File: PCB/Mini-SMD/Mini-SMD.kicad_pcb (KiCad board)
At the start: 2 copper layers, 65.1 x 96.9 mm, 31 parts, among them J1 Daisy port out, J2 2-pin header, J3 ICSP_ISP6, J4 Daisy port in, K1 HYC77-TF09-200, U1 PC817C-S, U2 ATmega328P-AU, U3 SE5218, U4 TXB0104PWR, Y1 Resonator_GND2

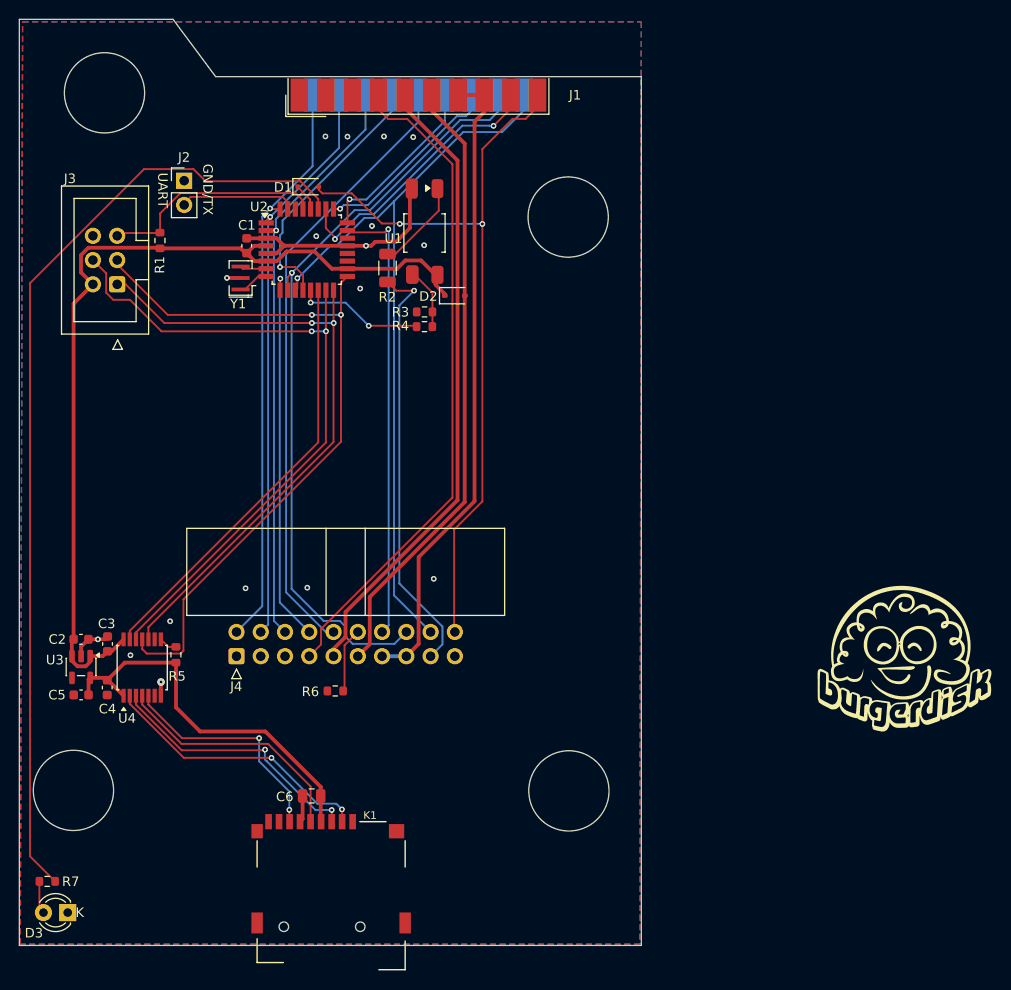
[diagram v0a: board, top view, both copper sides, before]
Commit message: Make PCBs closer to one another
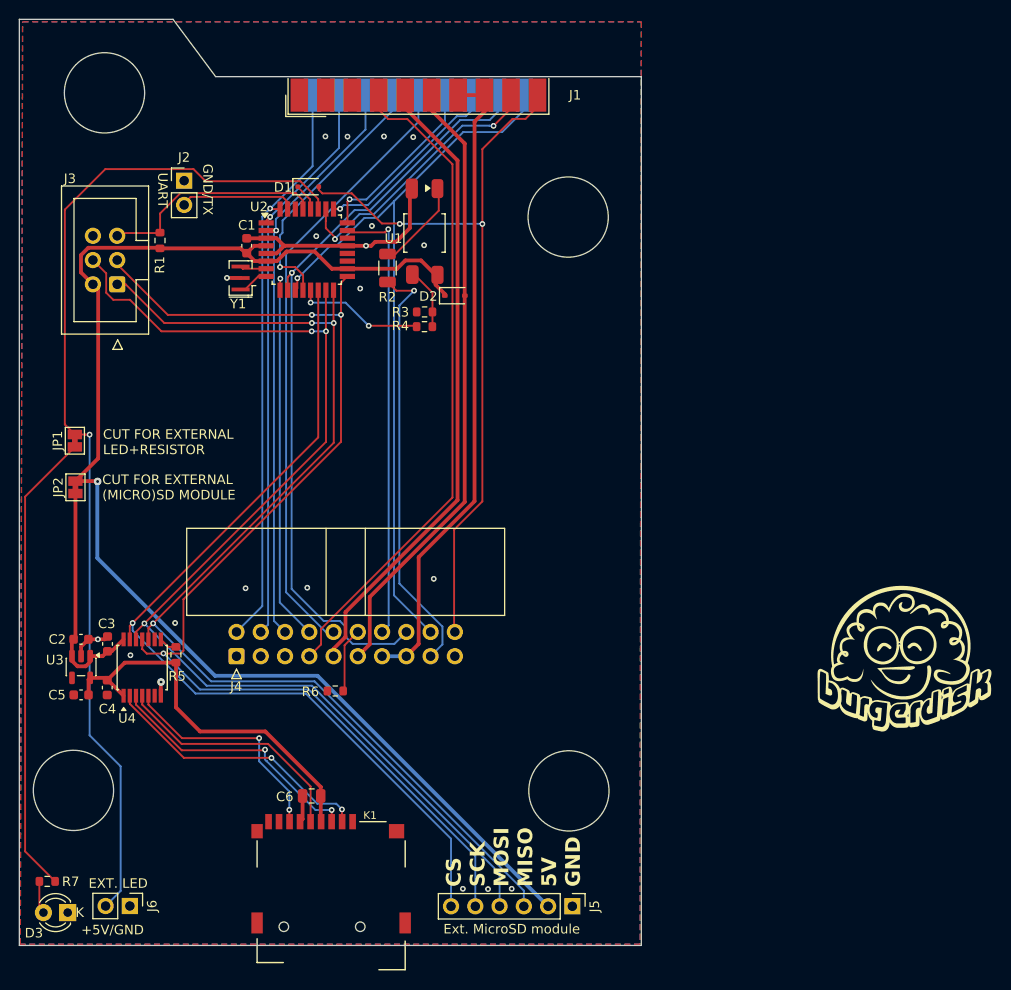
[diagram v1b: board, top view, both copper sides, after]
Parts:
- added J5: Ext. MicroSD module, Connector_PinHeader_2.54mm:PinHeader_1x06_P2.54mm_Vertical, F.Cu at (157.4, 136.2)
- added J6: 2-pin header, Connector_PinHeader_2.54mm:PinHeader_1x02_P2.54mm_Vertical, F.Cu at (111.1, 136.1)
- added JP1: INT/EXT LED JUMPER, Jumper:SolderJumper-2_P1.3mm_Bridged_Pad1.0x1.5mm, F.Cu at (105.3, 87.4)
- added JP2: INT MICROSD JUMPER, Jumper:SolderJumper-2_P1.3mm_Bridged_Pad1.0x1.5mm, F.Cu at (105.4, 92.3)
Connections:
- C2 pad 2: 5V_burgerDisk -> 5V_intMicroSD
- C3 pad 2: 5V_burgerDisk -> 5V_intMicroSD
- R7 pad 2: LED -> Net-(JP1-A)
- U3 pad 1: 5V_burgerDisk -> 5V_intMicroSD
- U3 pad 3: 5V_burgerDisk -> 5V_intMicroSD
- U4 pad 14: 5V_burgerDisk -> 5V_intMicroSD
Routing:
- net MISO: track 68.9 -> 121.0 mm, vias 2 -> 3
- net MOSI: track 73.5 -> 125.0 mm, vias 2 -> 3
- net CS: track 44.7 -> 95.0 mm, vias 0 -> 1
- net Net-(JP1-A): track 0.00 -> 49.5 mm
- net 5V_burgerDisk: track 95.9 -> 143.4 mm, vias 0 -> 1
- net SCK: track 78.0 -> 124.7 mm, vias 2 -> 3
- net 5V_intMicroSD: track 0.00 -> 24.2 mm
- net LED: track 101.2 -> 107.5 mm, vias 0 -> 1
- net GND: vias 17 -> 20
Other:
- board text added: "+5V/GND"
- board text added: "CS SCK MOSI MISO 5V GND"
- board text added: "CUT FOR EXTERNAL (MICRO)SD MODULE"
- board text added: "CUT FOR EXTERNAL LED+RESISTOR"
- board text added: "EXT. LED"
- board text added: "If using an external SD or MicroSD module, cut power to the internal one by cutting the trace in the JP2 jumper. If using an external LED (with external resistor), cut power to the internal one by cutting the trace in the JP1 jumper."

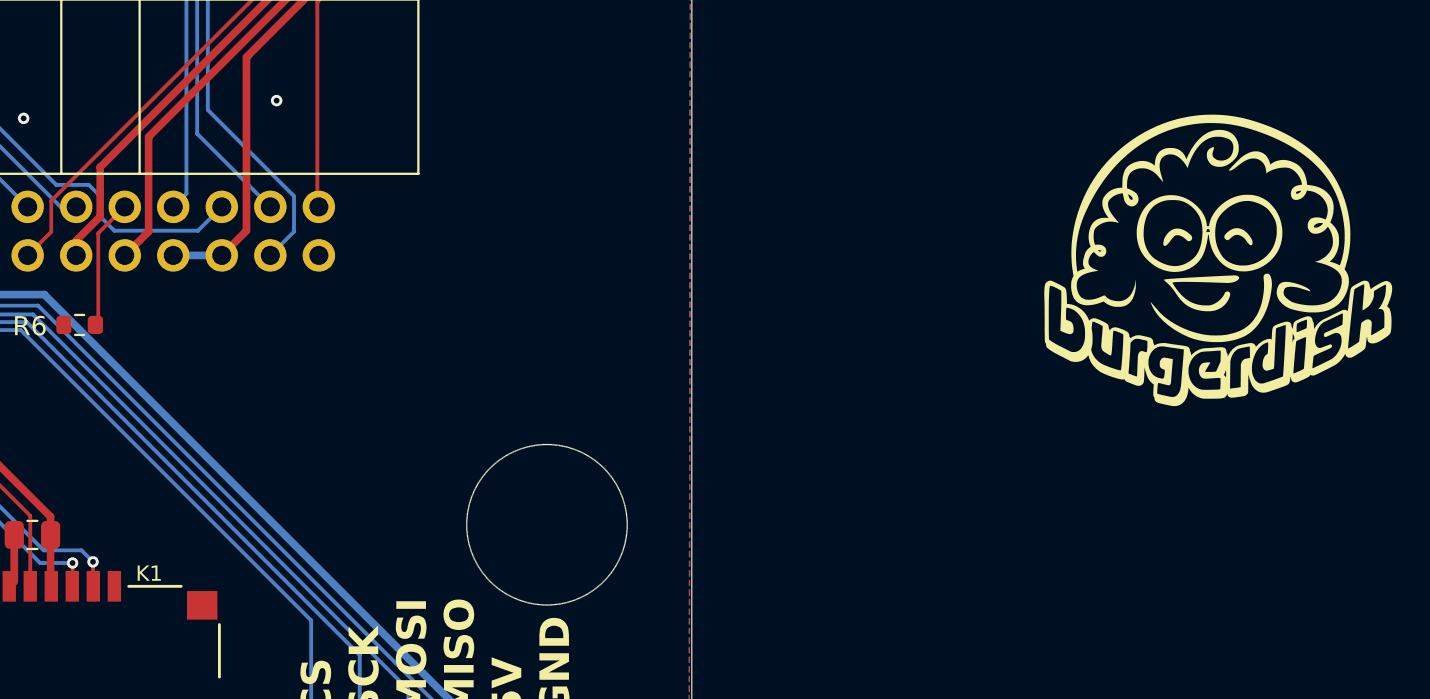
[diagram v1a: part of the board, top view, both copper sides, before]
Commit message: Put the logo back on the PCB
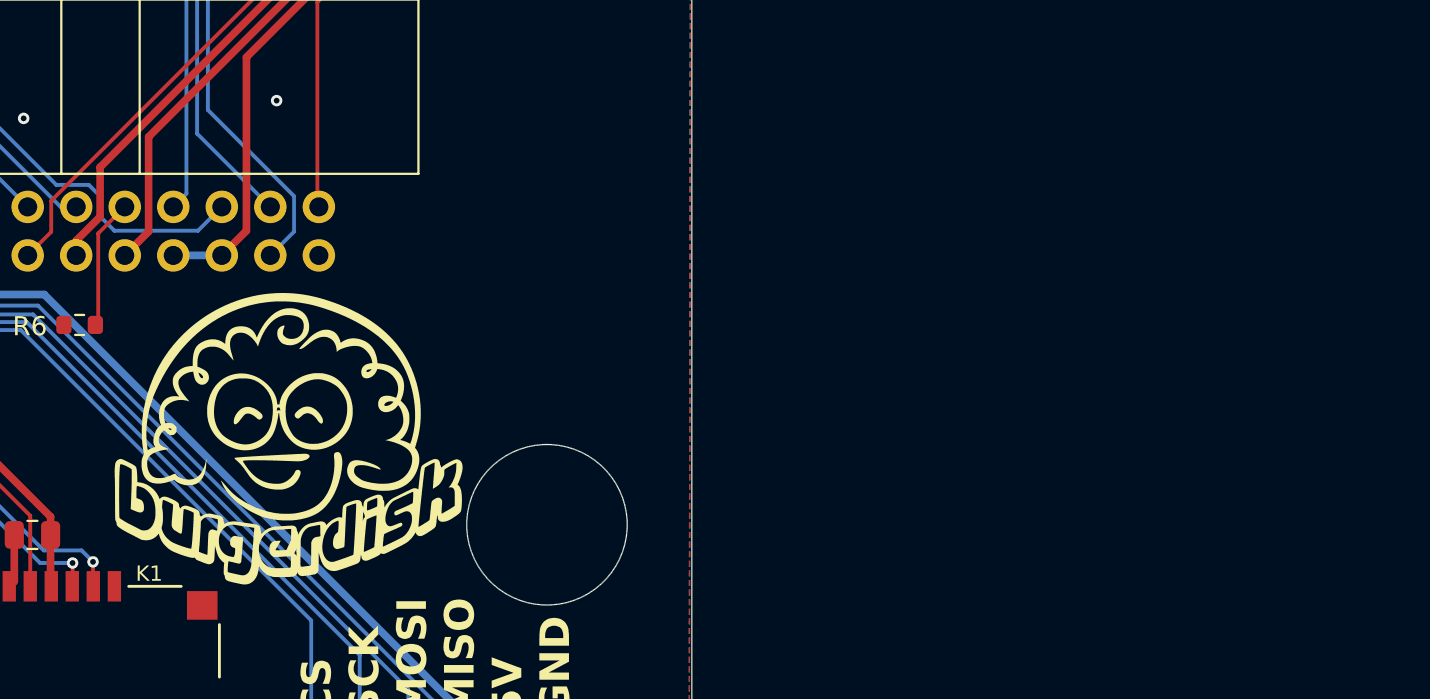
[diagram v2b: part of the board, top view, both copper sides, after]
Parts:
- moved G*** 49.5 mm to (143.5, 119.6)
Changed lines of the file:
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@@
 	(footprint "LOGO"
 		(layer "F.Cu")
-		(at 192.162905 110.299597)
+		(at 143.51 119.634)
 		(property "Reference" "G***"
 			(at 0 0 0)

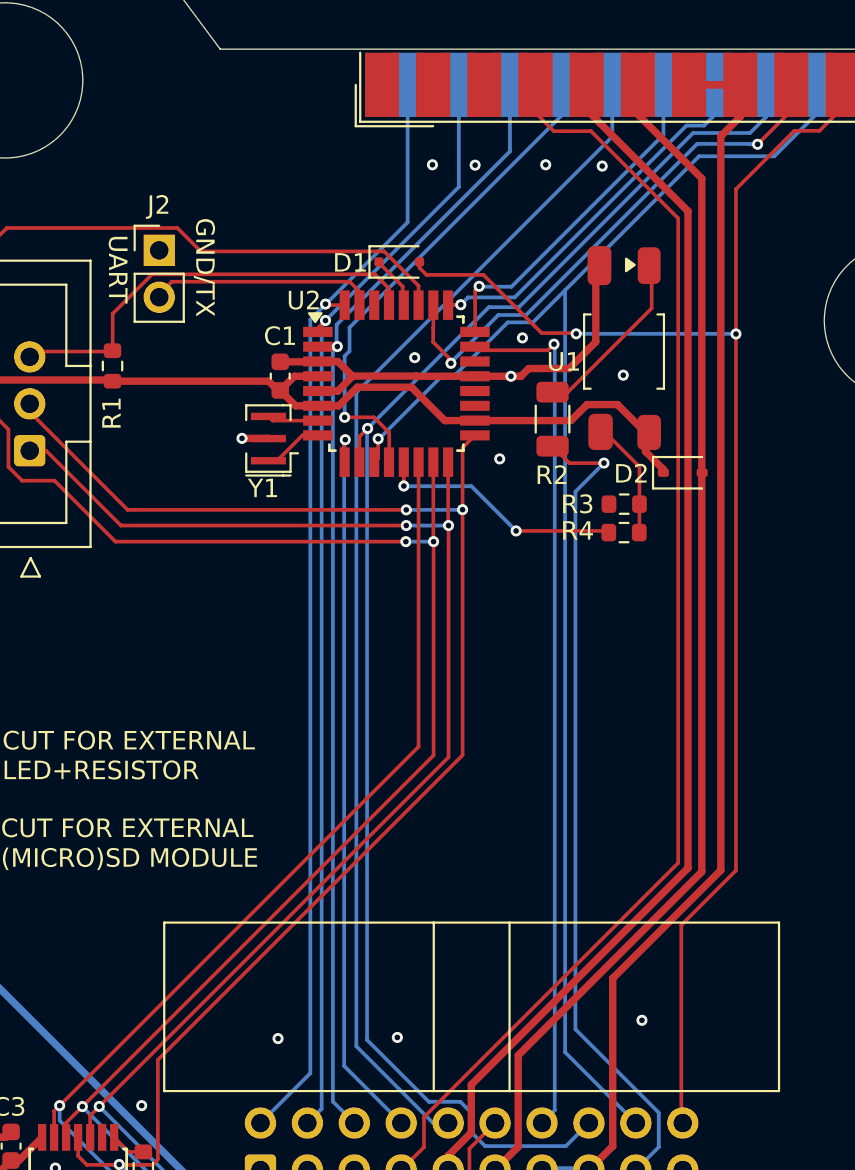
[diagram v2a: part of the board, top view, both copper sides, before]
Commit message: Move to bigger pads for diodes
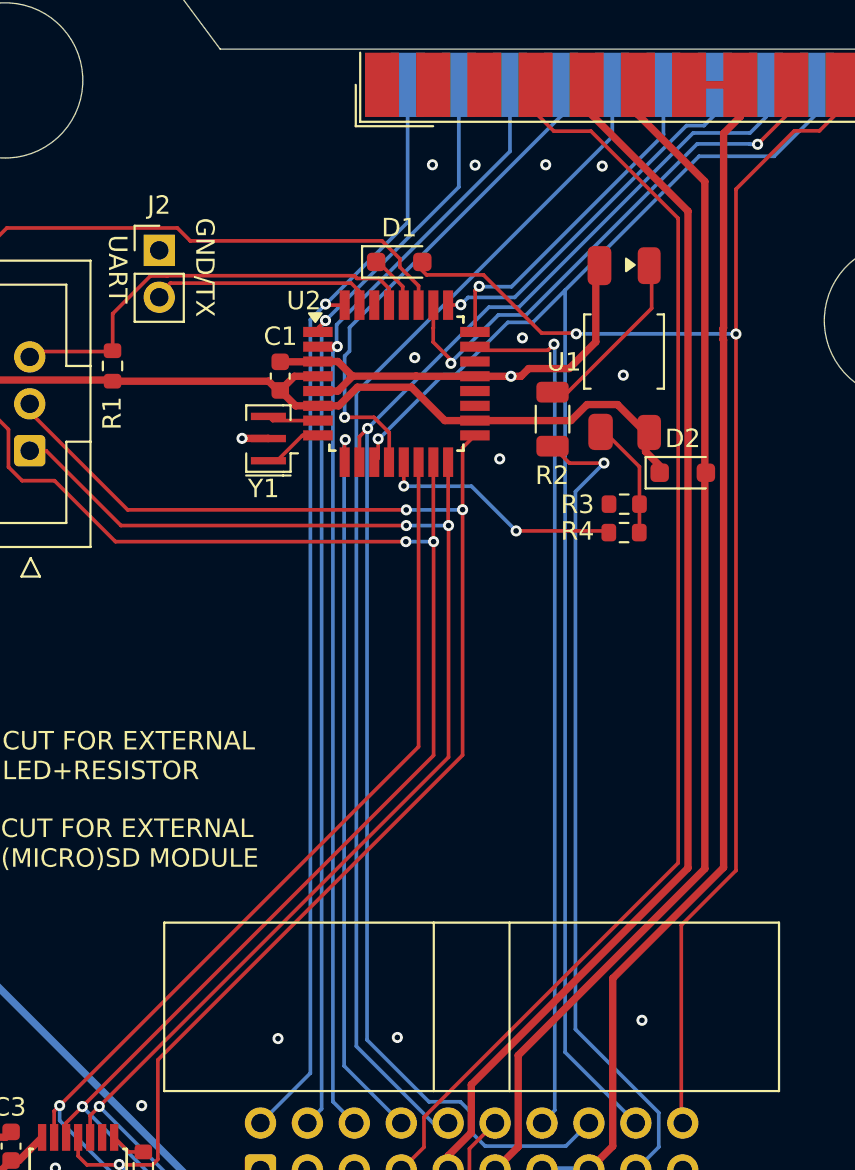
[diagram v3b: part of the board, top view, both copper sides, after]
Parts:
- D1: footprint Diode_SMD:D_SOD-323F -> Diode_SMD:D_SOD-323_HandSoldering
- D2: footprint Diode_SMD:D_SOD-323 -> Diode_SMD:D_SOD-323_HandSoldering
